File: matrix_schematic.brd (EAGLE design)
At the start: 83.5 x 84.4 mm, 25 parts, among them IC1 74LS595D, IC2 74LS595D, IC3 74LS595D, J1 AVR_SPI_PRG_6PTH, Q1 MOSFET-NCHANNELBS270, Q2 MOSFET-NCHANNELBS270, Q3 MOSFET-NCHANNELBS270, Q4 MOSFET-NCHANNELBS270

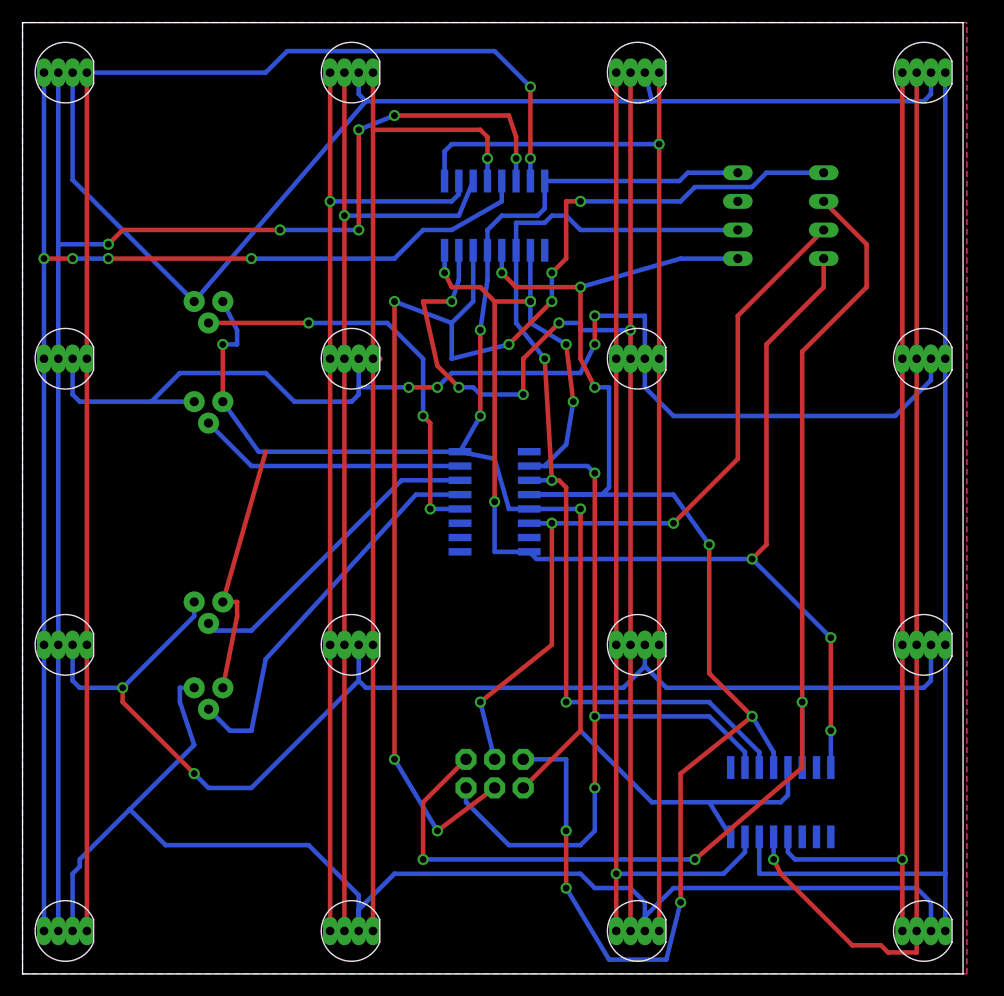
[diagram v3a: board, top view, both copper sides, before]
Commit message: Update design rules to use ITEADstudio DRC file
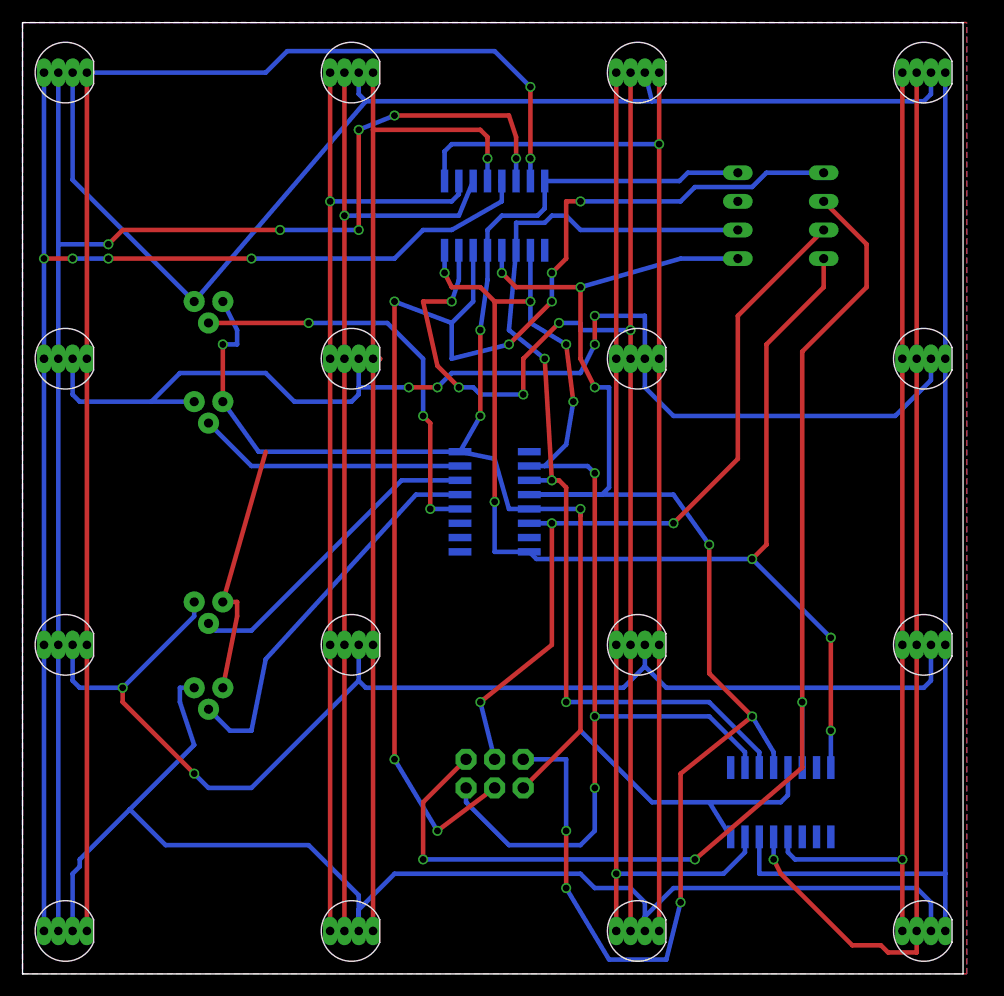
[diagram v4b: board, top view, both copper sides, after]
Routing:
- net N$3: track 87.2 -> 87.9 mm
- net VCC: vias 12 -> 11
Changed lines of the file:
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@@
 </class>
 </classes>
-<designrules name="default">
+<designrules name="ITEADstudio_DRC">
 <description language="de">&lt;b&gt;EAGLE Design Rules&lt;/b&gt;
 &lt;p&gt;
@@
 necessary adjustments and save your customized
 design rules under a new name.</description>
+<description language="zh">&lt;b&gt;Seeed Studio EAGLE Design Rules&lt;/b&gt;
+</description>
 <param name="layerSetup" value="(1*16)"/>
 <param name="mtCopper" value="0.035mm 0.035mm 0.035mm 0.035mm 0.035mm 0.035mm 0.035mm 0.035mm 0.035mm 0.035mm 0.035mm 0.035mm 0.035mm 0.035mm 0.035mm 0.035mm"/>
 <param name="mtIsolate" value="1.5mm 0.15mm 0.2mm 0.15mm 0.2mm 0.15mm 0.2mm 0.15mm 0.2mm 0.15mm 0.2mm 0.15mm 0.2mm 0.15mm 0.2mm"/>
-<param name="mdWireWire" value="8mil"/>
-<param name="mdWirePad" value="8mil"/>
-<param name="mdWireVia" value="8mil"/>
-<param name="mdPadPad" value="8mil"/>
-<param name="mdPadVia" value="8mil"/>
-<param name="mdViaVia" value="8mil"/>
-<param name="mdSmdPad" value="8mil"/>
-<param name="mdSmdVia" value="8mil"/>
-<param name="mdSmdSmd" value="8mil"/>
+<param name="mdWireWire" value="6mil"/>
+<param name="mdWirePad" value="6mil"/>
+<param name="mdWireVia" value="6mil"/>
+<param name="mdPadPad" value="6mil"/>
+<param name="mdPadVia" value="6mil"/>
+<param name="mdViaVia" value="6mil"/>
+<param name="mdSmdPad" value="0mil"/>
+<param name="mdSmdVia" value="0mil"/>
+<param name="mdSmdSmd" value="0mil"/>
 <param name="mdViaViaSameLayer" value="8mil"/>
 <param name="mnLayersViaInSmd" value="2"/>
-<param name="mdCopperDimension" value="40mil"/>
-<param name="mdDrill" value="8mil"/>
+<param name="mdCopperDimension" value="10mil"/>
+<param name="mdDrill" value="10mil"/>
 <param name="mdSmdStop" value="0mil"/>
-<param name="msWidth" value="10mil"/>
-<param name="msDrill" value="24mil"/>
-<param name="msMicroVia" value="9.99mm"/>
+<param name="msWidth" value="6mil"/>
+<param name="msDrill" value="12mil"/>
+<param name="msMicroVia" value="12mil"/>
 <param name="msBlindViaRatio" value="0.5"/>
 <param name="rvPadTop" value="0.25"/>
@@
 <param name="rlMinPadBottom" value="10mil"/>
 <param name="rlMaxPadBottom" value="20mil"/>
-<param name="rlMinViaOuter" value="8mil"/>
+<param name="rlMinViaOuter" value="6mil"/>
 <param name="rlMaxViaOuter" value="20mil"/>
-<param name="rlMinViaInner" value="8mil"/>
+<param name="rlMinViaInner" value="6mil"/>
 <param name="rlMaxViaInner" value="20mil"/>
 <param name="rlMinMicroViaOuter" value="4mil"/>
@@
 <param name="psTop" value="-1"/>
 <param name="psBottom" value="-1"/>
-<param name="psFirst" value="-1"/>
+<param name="psFirst" value="0"/>
 <param name="psElongationLong" value="100"/>
 <param name="psElongationOffset" value="100"/>
 <param name="mvStopFrame" value="1"/>
 <param name="mvCreamFrame" value="0"/>
-<param name="mlMinStopFrame" value="4mil"/>
-<param name="mlMaxStopFrame" value="4mil"/>
+<param name="mlMinStopFrame" value="2mil"/>
+<param name="mlMaxStopFrame" value="2mil"/>
 <param name="mlMinCreamFrame" value="0mil"/>
 <param name="mlMaxCreamFrame" value="0mil"/>
-<param name="mlViaStopLimit" value="0mil"/>
+<param name="mlViaStopLimit" value="100mil"/>
 <param name="srRoundness" value="0"/>
 <param name="srMinRoundness" value="0mil"/>
@@
 <param name="checkAngle" value="0"/>
 <param name="checkFont" value="1"/>
-<param name="checkRestrict" value="1"/>
+<param name="checkRestrict" value="0"/>
 <param name="useDiameter" value="13"/>
 <param name="maxErrors" value="50"/>
@@
 <wire x1="41.91" y1="58.42" x2="45.085" y2="58.42" width="0.4064" layer="1"/>
 <via x="45.085" y="58.42" extent="1-16" drill="0.6" shape="square"/>
-<via x="45.085" y="58.42" extent="1-16" drill="0.6" shape="square"/>
 <contactref element="J1" pad="2"/>
 <wire x1="39.37" y1="15.24" x2="39.37" y2="13.97" width="0.4064" layer="16"/>
@@
 <via x="48.26" y="22.86" extent="1-16" drill="0.6" shape="square"/>
 <wire x1="48.26" y1="22.86" x2="48.26" y2="41.91" width="0.4064" layer="1"/>
-<wire x1="43.815" y1="56.515" x2="46.355" y2="53.34" width="0.4064" layer="16"/>
+<wire x1="43.18" y1="55.88" x2="46.355" y2="53.34" width="0.4064" layer="16"/>
 <via x="46.355" y="53.34" extent="1-16" drill="0.6" shape="square"/>
 <wire x1="46.355" y1="53.34" x2="46.99" y2="42.545" width="0.4064" layer="1"/>
@@
 <wire x1="46.99" y1="66.04" x2="46.355" y2="65.405" width="0.4064" layer="16"/>
 <wire x1="46.355" y1="65.405" x2="43.815" y2="65.405" width="0.4064" layer="16"/>
-<wire x1="43.815" y1="56.515" x2="43.815" y2="62.9666" width="0.4064" layer="16"/>
+<wire x1="43.18" y1="55.88" x2="43.815" y2="62.9666" width="0.4064" layer="16"/>
 <wire x1="43.815" y1="65.405" x2="43.815" y2="62.9666" width="0.4064" layer="16"/>
 <wire x1="44.9834" y1="42.545" x2="46.99" y2="42.545" width="0.4064" layer="16"/>
